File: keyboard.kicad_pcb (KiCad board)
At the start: 2 copper layers, 228 x 75.8 mm, 194 parts, among them IC1 ATMEGA32U4, J1 MINI, P1 MISO, P10 ROW4, P18 LR1, P19 LR2, P2 Vcc, P20 LR3, P200 GND, P201 GND, P202 GND, P203 GND, P21 LR4, P23 LC1, P24 LC2, P25 LC3, P26 LC4, P27 LC5, P28 LC6, P29 LC7, P3 SCK, P30 LC8, P31 LC9, P32 LC10, P33 LC11, P34 LC12, P35 LGND, P36 LVcc, P37 Vcc, P38 GPIO0, P39 GPIO1, P4 MOSI, P40 GPIO2, P41 GPIO3, P42 GPIO4(SS), P43 GPIO5(SCK), P44 GPIO6(MOSI), P45 GPIO7(SCL), P46 GPIO8(SDA), P47 GND, P5 RES, P6 GND, P7 ROW1, P8 ROW2, P9 ROW3, X1 ASX3F

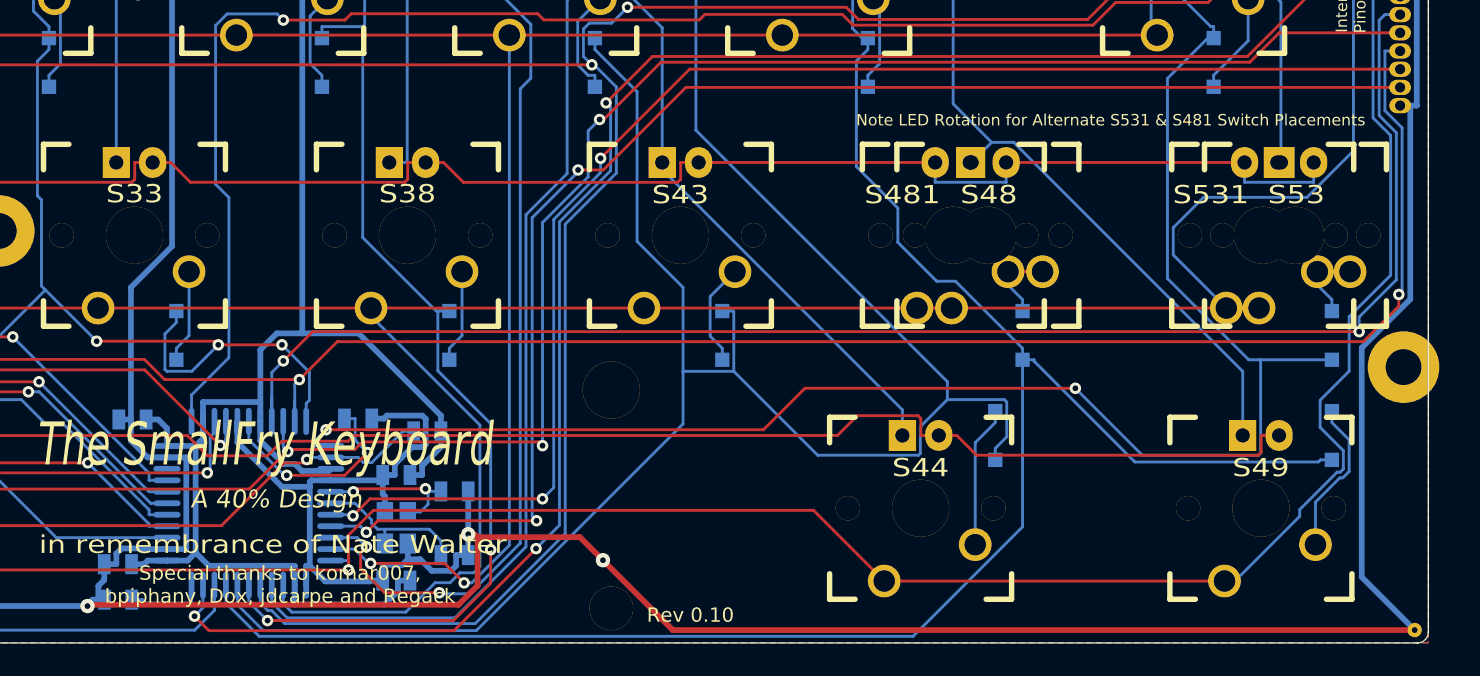
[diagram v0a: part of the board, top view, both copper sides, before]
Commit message: Change the cyrstal footprint / correct two wrong diode directions
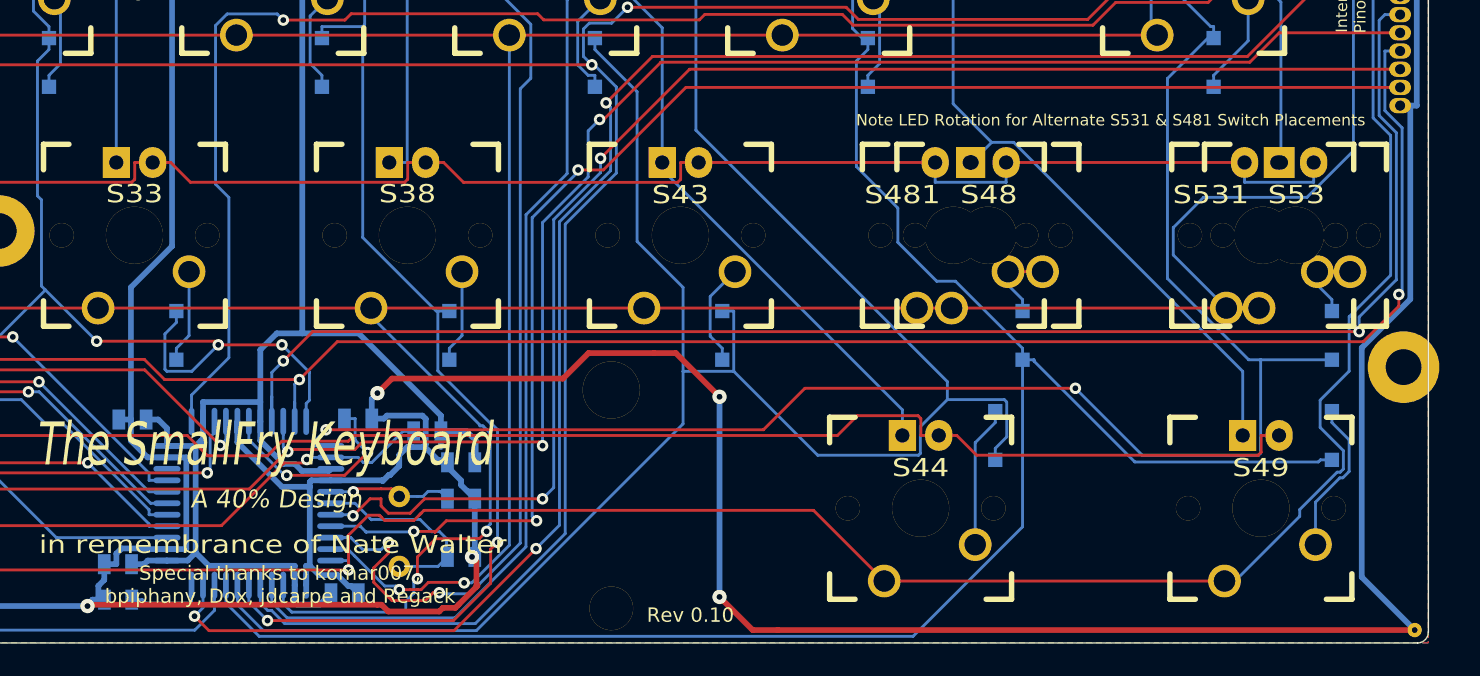
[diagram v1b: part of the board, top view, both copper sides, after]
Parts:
- X1: value ASX3F -> CRYSTAL; footprint ASX3F -> Crystals:Crystal_HC49-U_Vertical
- moved C7 4.61 mm to (222.8, 127.8)
- moved C6 3.71 mm to (214.6, 136.9), turned to 0 degrees
- moved C1 0.68 mm to (222.8, 130.3)
- moved C2 0.47 mm to (222.8, 134.4)
- moved X1 0.33 mm to (218.4, 132.6)
- turned D48 to 90 degrees
- turned D53 to 90 degrees
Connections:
- C2 pad 1: N-000001 -> Net-(C2-Pad1)
- D48 pad 1: N-0000093 -> /Matrix/col10
- D48 pad 2: /Matrix/col10 -> Net-(D48-Pad2)
- D53 pad 1: N-0000094 -> /Matrix/col11
- D53 pad 2: /Matrix/col11 -> Net-(D53-Pad2)
- IC1 pad 17: N-000001 -> Net-(C2-Pad1)
- IC1 pad 42: (no net) -> Net-(IC1-Pad42)
- J1 pad 4: (no net) -> Net-(J1-Pad4)
- S0 pad 2: (no net) -> Net-(S0-Pad2)
- S0 pad 4: (no net) -> Net-(S0-Pad4)
- S48 pad 2: N-0000093 -> Net-(D48-Pad2)
- S481 pad 2: N-0000093 -> Net-(D48-Pad2)
- S53 pad 2: N-0000094 -> Net-(D53-Pad2)
- S531 pad 2: N-0000094 -> Net-(D53-Pad2)
- X1 pad 2: GND -> Net-(C2-Pad1)
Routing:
- net Net-(C2-Pad1): track 0.00 -> 14.4 mm
- net GND: track 789.6 -> 802.4 mm, vias 26 -> 28
- net N-000001: track 11.9 -> 0.00 mm
- net Net-(D48-Pad2): track 0.00 -> 5.58 mm
- net N-0000093: track 5.58 -> 0.00 mm
- net VCC: track 472.4 -> 467.0 mm
- net Net-(D53-Pad2): track 0.00 -> 5.46 mm
- net N-0000094: track 5.46 -> 0.00 mm
- net /Matrix/row1: track 298.3 -> 300.8 mm
- net /Matrix/row3: track 284.4 -> 285.8 mm, vias 0 -> 2
- net /GPIO7: track 99.1 -> 100.2 mm
- net Net-(C1-Pad1): track 10.4 -> 9.32 mm, vias 2 -> 1

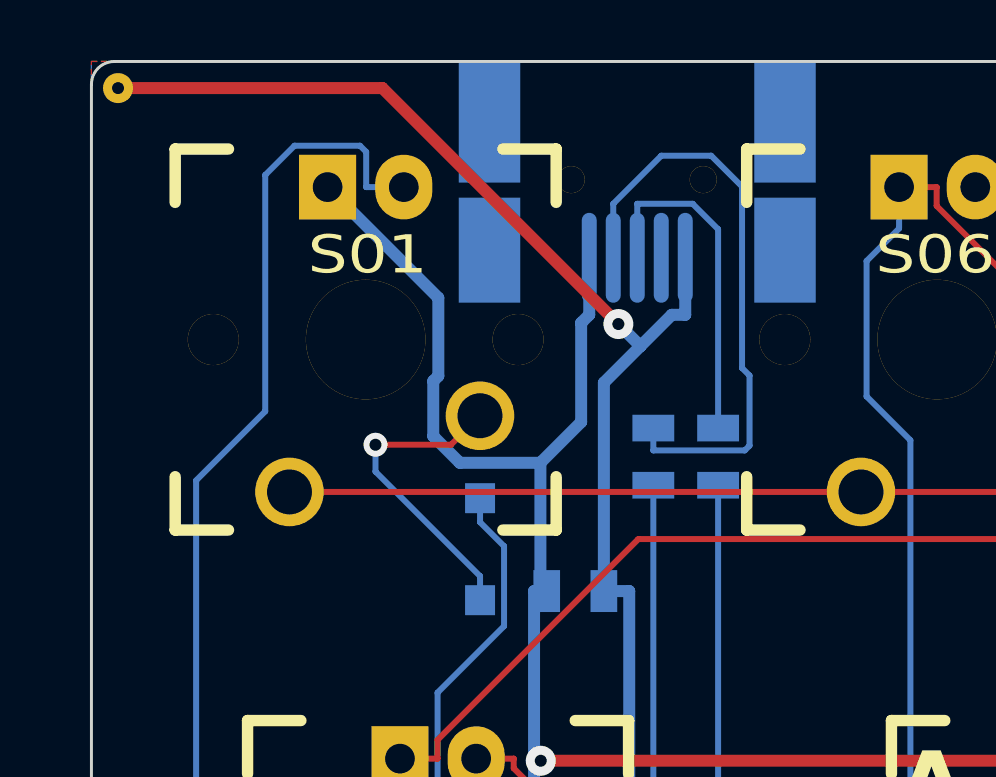
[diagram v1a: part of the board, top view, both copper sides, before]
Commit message: Change the footprint of MiniUSB
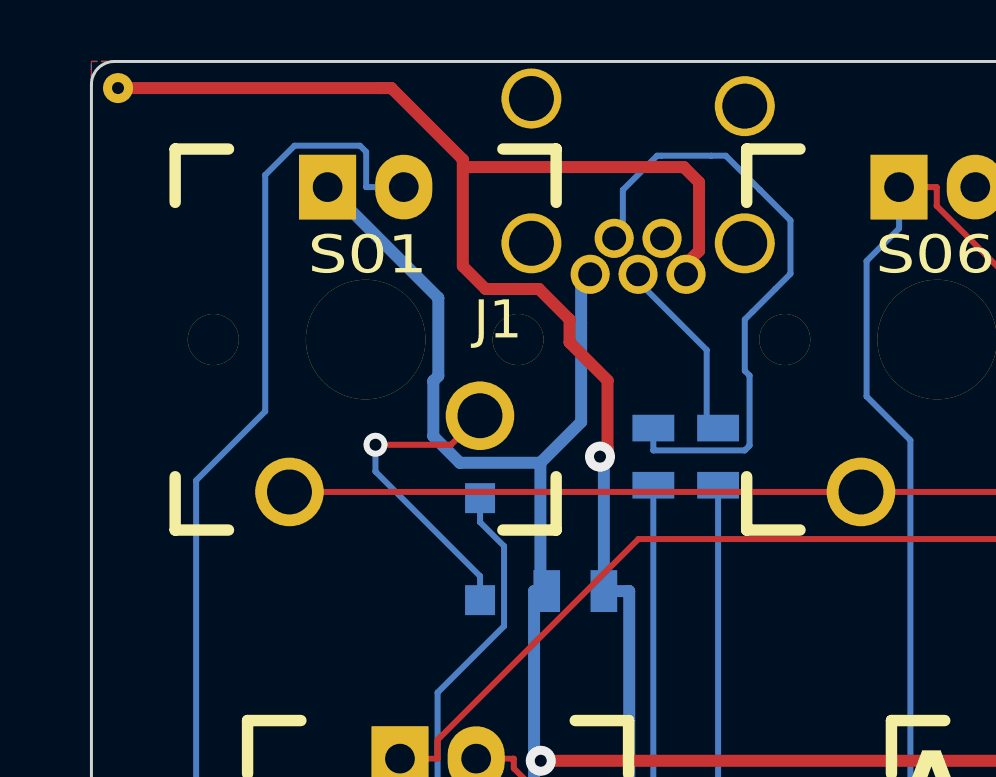
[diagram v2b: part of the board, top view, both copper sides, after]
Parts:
- J1: footprint USB_MINI-B_MOLEX_67503-1020 -> USB:DX_USB
- moved J1 1.96 mm to (80.5, 66.5), turned to 270 degrees
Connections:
- net Net-(J1-Pad2) renamed /D-
- net Net-(J1-Pad3) renamed /D+
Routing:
- net GND: track 802.4 -> 810.8 mm
- net /D+: track 11.5 -> 6.23 mm
- net /D-: track 19.9 -> 20.9 mm
